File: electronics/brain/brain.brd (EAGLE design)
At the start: 53.3 x 59.7 mm, 5 parts, among them U1 SC0918

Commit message: Fixed power issue in current iteration of boards.
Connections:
- removed net 15: U$4.15
- net VCC: now also U$4.15
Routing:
- net VCC: track 107.8 -> 115.4 mm, vias 2 -> 3
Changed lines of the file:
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@@
 <wire x1="3.81" y1="20.32" x2="11.43" y2="20.32" width="1.016" layer="1"/>
 <via x="11.43" y="20.32" extent="1-16" drill="0.35"/>
-<wire x1="11.43" y1="20.32" x2="11.43" y2="3.81" width="1.016" layer="16"/>
+<wire x1="11.43" y1="20.32" x2="11.43" y2="12.7" width="1.016" layer="16"/>
+<wire x1="11.43" y1="12.7" x2="11.43" y2="3.81" width="1.016" layer="16"/>
 <wire x1="11.43" y1="3.81" x2="11.66" y2="3.81" width="0.254" layer="16"/>
 <wire x1="11.66" y1="3.81" x2="23.495" y2="3.81" width="1.016" layer="16"/>
@@
 <wire x1="26.035" y1="40.64" x2="30.48" y2="40.64" width="1.016" layer="16"/>
 <wire x1="30.48" y1="40.64" x2="31.75" y2="41.91" width="1.016" layer="16"/>
-<wire x1="31.75" y1="41.91" x2="31.75" y2="47.625" width="1.016" layer="16"/>
+<wire x1="31.75" y1="41.91" x2="31.75" y2="48.26" width="1.016" layer="16"/>
 <via x="31.75" y="54.61" extent="1-16" drill="0.35"/>
 <wire x1="31.75" y1="48.26" x2="31.75" y2="54.61" width="1.016" layer="16"/>
 <wire x1="31.75" y1="54.61" x2="36.36" y2="54.61" width="1.016" layer="1"/>
-<wire x1="31.75" y1="47.625" x2="31.75" y2="48.26" width="1.016" layer="16"/>
 <wire x1="31.75" y1="48.26" x2="41.91" y2="48.26" width="1.016" layer="16"/>
+<contactref element="U$4" pad="15"/>
+<via x="11.43" y="12.7" extent="1-16" drill="0.35"/>
+<wire x1="11.43" y1="12.7" x2="3.81" y2="12.7" width="1.016" layer="1"/>
 </signal>
 <signal name="AGND">
@@
 <via x="10.16" y="30.48" extent="1-16" drill="0.35"/>
 </signal>
-<signal name="15">
-<contactref element="U$4" pad="15"/>
-</signal>
 <signal name="18">

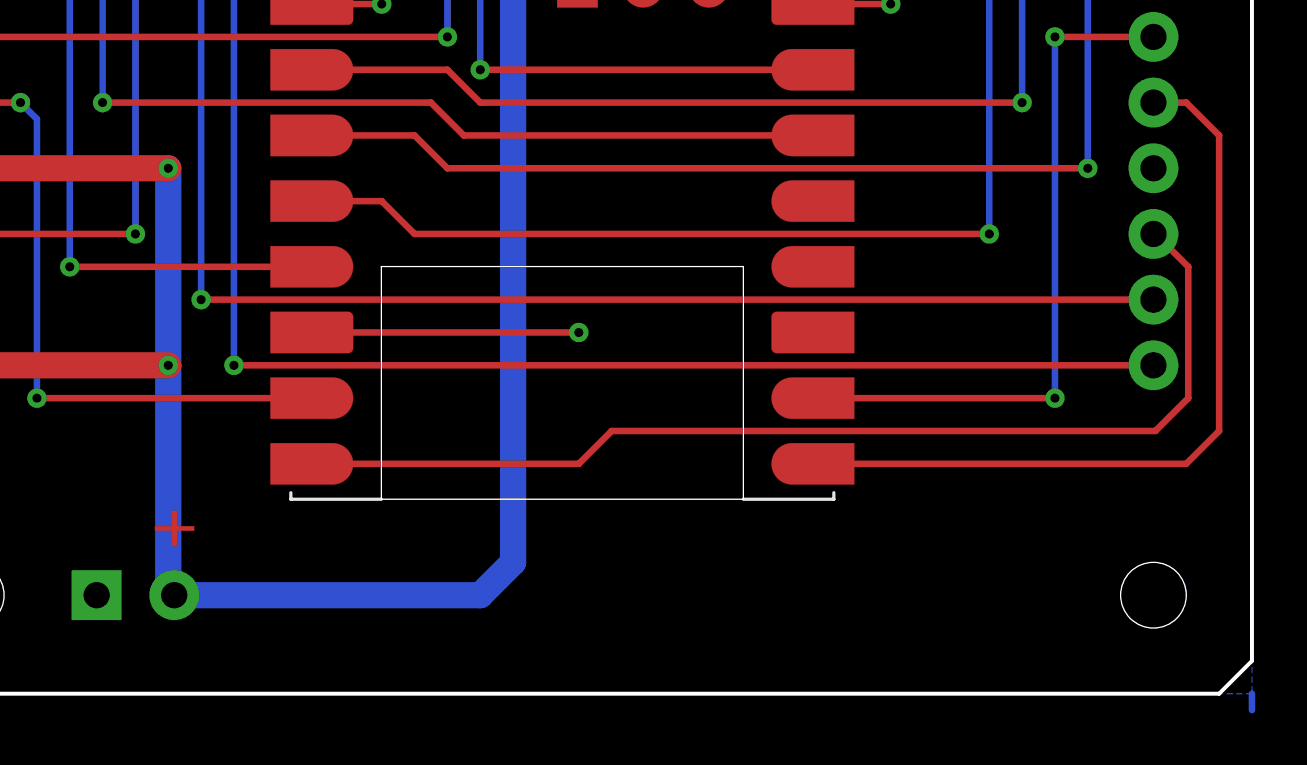
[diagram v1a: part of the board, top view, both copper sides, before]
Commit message: Removed fragment on border. Changed vias on VCC to same diameter as traces (40 mil).
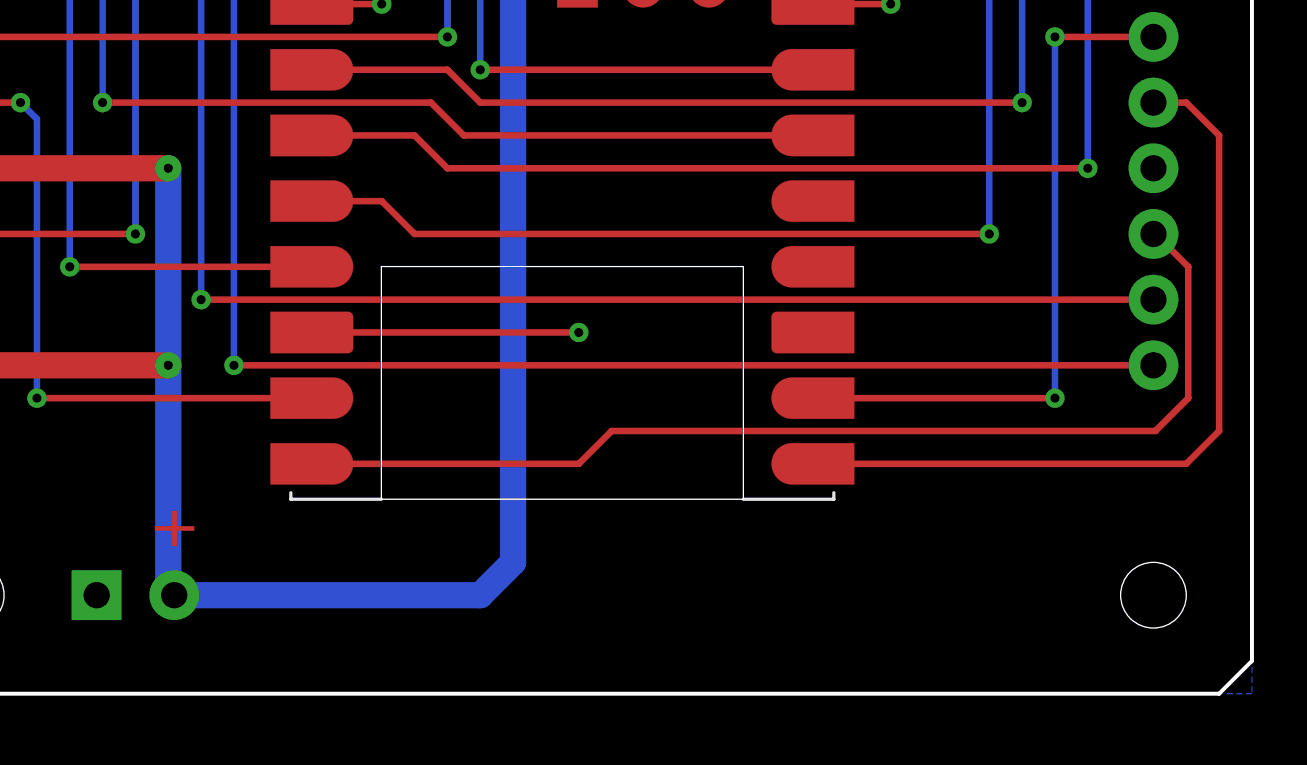
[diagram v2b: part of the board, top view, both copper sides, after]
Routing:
- net GND: track 31.2 -> 30.6 mm
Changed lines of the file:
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@@
 <via x="27.305" y="13.97" extent="1-16" drill="0.35"/>
 <wire x1="16.98" y1="13.97" x2="27.305" y2="13.97" width="0.254" layer="1"/>
-<wire x1="53.34" y1="0" x2="53.34" y2="-0.635" width="0.254" layer="16"/>
 <polygon width="0.254" layer="16">
 <vertex x="53.34" y="0"/>
@@
 <wire x1="8.89" y1="3.81" x2="16.98" y2="13.97" width="0" layer="19" extent="1-1"/>
 <wire x1="3.81" y1="15.24" x2="8.66" y2="3.81" width="0" layer="19" extent="1-1"/>
-<wire x1="53.34" y1="0" x2="49.53" y2="20.32" width="0" layer="19" extent="16-16"/>
 </signal>
 <signal name="+3V3">
@@
 <contactref element="C1" pad="1"/>
 <wire x1="3.81" y1="20.32" x2="11.43" y2="20.32" width="1.016" layer="1"/>
-<via x="11.43" y="20.32" extent="1-16" drill="0.35"/>
+<via x="11.43" y="20.32" extent="1-16" drill="0.35" diameter="1.016"/>
 <wire x1="11.43" y1="20.32" x2="11.43" y2="12.7" width="1.016" layer="16"/>
 <wire x1="11.43" y1="12.7" x2="11.43" y2="3.81" width="1.016" layer="16"/>
@@
 <wire x1="31.75" y1="48.26" x2="41.91" y2="48.26" width="1.016" layer="16"/>
 <contactref element="U$4" pad="15"/>
-<via x="11.43" y="12.7" extent="1-16" drill="0.35"/>
+<via x="11.43" y="12.7" extent="1-16" drill="0.35" diameter="1.016"/>
 <wire x1="11.43" y1="12.7" x2="3.81" y2="12.7" width="1.016" layer="1"/>
 </signal>
